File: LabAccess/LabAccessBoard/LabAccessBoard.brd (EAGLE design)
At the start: 43.2 x 62.2 mm, 26 parts, among them CN1 6p-2.54, Q1 AO3400, X1 1751248

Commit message: board update
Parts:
- removed C4: 100nF, rcl:C0603K
- removed CN1: 6p-2.54, Seeed-Connector:H6-2.54
- removed R1, R2, R7: 10k, resistor:R0603
- added J1: 4p-2.54, Seeed-Connector:H4-2.54
- moved R3 14.3 mm to (26.4, 32.7), turned to 0 degrees
- moved R6 8.80 mm to (26.4, 35.2), turned to 0 degrees
- moved C3 5.12 mm to (21.9, 38.4), turned to 90 degrees
- moved Q1 3.82 mm to (22.2, 26.7), turned to 90 degrees
- moved C1 2.86 mm to (22.2, 32.7), turned to 0 degrees
- moved D1 1.59 mm to (18.4, 30.8)
- moved R5 0.63 mm to (22.2, 30.2), turned to 180 degrees
- moved C6 0.32 mm to (26.4, 30.2)
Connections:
- removed net EN: C4.2, R7.2, U1.CH_PD
- removed net GPIO0: C4.1, CN1.6, R2.2, U1.GPIO0
- removed net RST: JP1.7, U1.RESET
- new net EXTSW: R6.2, U1.GPIO5, X1.2
- net +3V3: now also J1.4; no longer CN1.3, R2.1, R7.1
- net CS: now also U1.GPIO16; no longer R1.2, U1.GPIO15
- net GND: now also J1.1; no longer CN1.1, R1.1
- net RLY: now also U1.GPIO15; no longer U1.GPIO16
- net RX: now also J1.2; no longer CN1.4
- net SW: now also U1.GPIO0; no longer R6.2, U1.GPIO5, X1.2
- net TX: now also J1.3; no longer CN1.5
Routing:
- net EXTSW: track 0.00 -> 41.7 mm, vias 0 -> 1
- net SW: track 101.3 -> 67.7 mm
- net GPIO0: track 29.2 -> 0.00 mm
- net EN: track 23.5 -> 0.00 mm
- net RX: track 29.2 -> 22.6 mm
- net RLY: track 27.8 -> 32.6 mm
- net CS: track 63.5 -> 59.4 mm, vias 1 -> 2
- net N$8: track 13.5 -> 16.8 mm
- net TX: track 31.2 -> 28.1 mm
- net GPIO2: track 16.0 -> 18.4 mm
- net +3V3: track 71.6 -> 69.7 mm
- net N$5: track 28.4 -> 29.2 mm
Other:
- board text added: "3V3"
- board text added: "BOOT"
- board text added: "GND"
- board text added: "RX"
- board text added: "TX"

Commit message: board update
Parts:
- added IC1: TLP281, TLP281(GB-TP_F):SOIC127P700X190-4N
- added R1: (no value), resistor:R0603
- added R2, R7: 0, resistor:R0603
- C5: value (none) -> 100nF
- HLK-PM03: value HLK-PM013W -> HLK-PM03
- R4: value S07K250 -> 250V
- R5: value 2ohm -> 2R
- U$1: value SRD-0XVDC-SL-CSRD-06VDC-SL-C -> SRD-03VDC-SL-C
- U$2: value (none) -> 10mH
- moved C3 3.19 mm to (22.2, 35.2), turned to 0 degrees
- renumbered HLK1 to HLK-PM03
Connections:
- new net A: IC1.1, R2.1, X1.2
- new net K: IC1.2, R1.2, R7.1
- new net K': R1.1, X1.1
- net EXTSW: now also IC1.4, R2.2; no longer X1.2
- net GND: now also IC1.3, R7.2; no longer X1.1
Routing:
- net A: track 0.00 -> 33.6 mm, vias 0 -> 1
- net K: track 0.00 -> 26.1 mm, vias 0 -> 2
- net K': track 0.00 -> 6.71 mm
- net SW: track 67.7 -> 71.6 mm
- net GPIO2: track 18.4 -> 22.1 mm
- net EXTSW: track 41.7 -> 43.2 mm, vias 1 -> 2
- net IRQ: track 59.3 -> 58.0 mm
- net N$2: track 80.7 -> 81.2 mm
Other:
- outline, holes or cut-outs redrawn
- board text added: "+"
- board text added: "-"
- board text added: "F 0.5A"
- board text removed: "F125mA"

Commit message: board update
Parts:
- removed C3: 100nF, rcl:C0603K
- C1, C6: value 22uF -> 1uF; device rcl:C0805K -> rcl:C0603K
- C2: value 22uF -> 10uF
- D1: value 1N4007 -> 1N4001
- R1: value (none) -> ROC
- R6: value 3.3k -> RSW
- moved C6 5.40 mm to (26.4, 35.6)
- moved R5 5.40 mm to (22.2, 35.6)
- moved C2 4.45 mm to (40.3, 1.91)
- moved R3 3.18 mm to (26.4, 29.5)
- moved Q1 2.86 mm to (22.2, 29.5)
- moved R6 2.54 mm to (26.4, 32.7)
- moved IC1 0.48 mm to (34.0, 32.2)
- moved R2 0.48 mm to (34.9, 32.2)
- moved R7 0.48 mm to (33.0, 32.2)
- moved D1 0.45 mm to (18.1, 31.1)
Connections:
- removed net K': R1.1, X1.1
- new net N$9: R1.1, X1.2
- net +3V3: no longer C3.2
- net A: now also R1.2; no longer X1.2
- net GND: no longer C3.1
- net K: now also X1.1; no longer R1.2
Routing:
- net K: track 26.1 -> 38.0 mm, vias 2 -> 1
- net K': track 6.71 -> 0.00 mm
- net N$9: track 0.00 -> 6.18 mm
- net A: track 33.6 -> 29.9 mm, vias 1 -> 2
- net +3V3: track 69.6 -> 66.1 mm
- net GPIO2: track 22.1 -> 25.3 mm
- net EXTSW: track 43.2 -> 46.2 mm
- net N$8: track 16.8 -> 15.0 mm
- net RLY: track 32.6 -> 34.2 mm
- net N$5: track 28.9 -> 30.3 mm

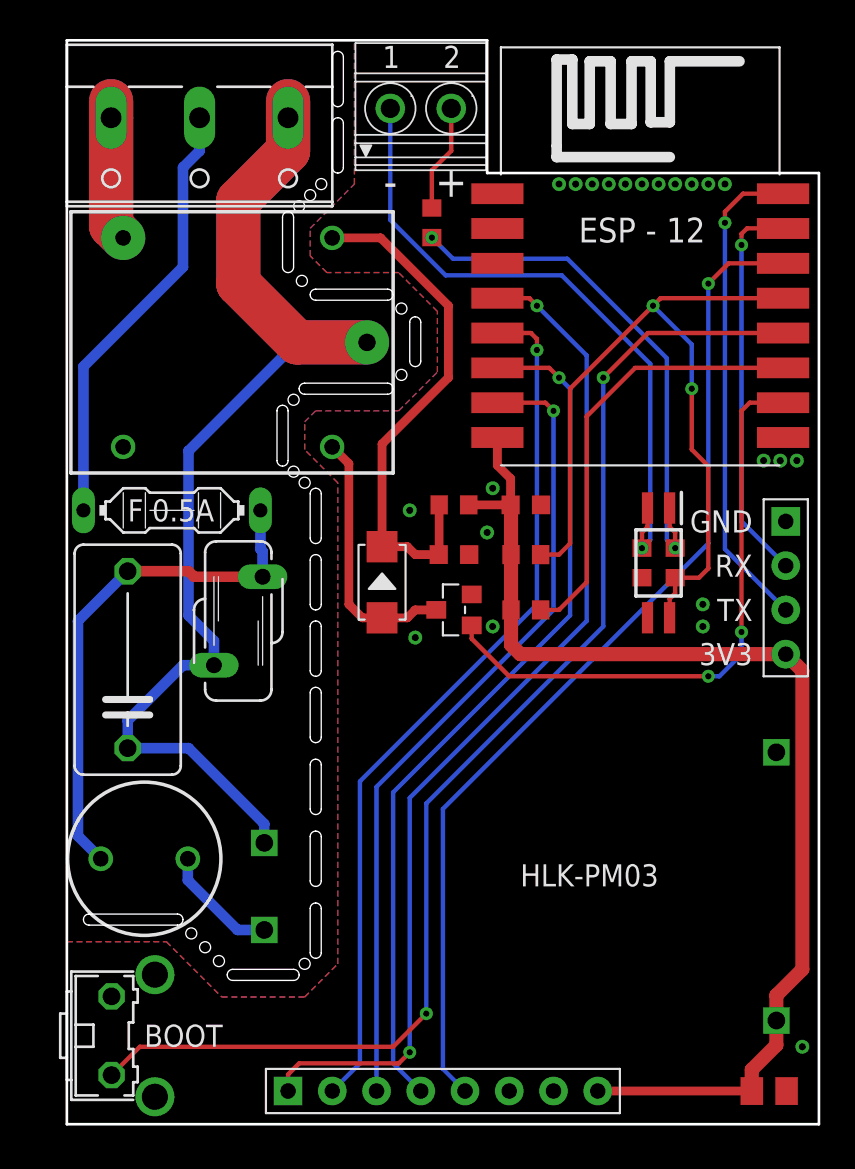
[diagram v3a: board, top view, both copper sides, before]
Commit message: new lab access board
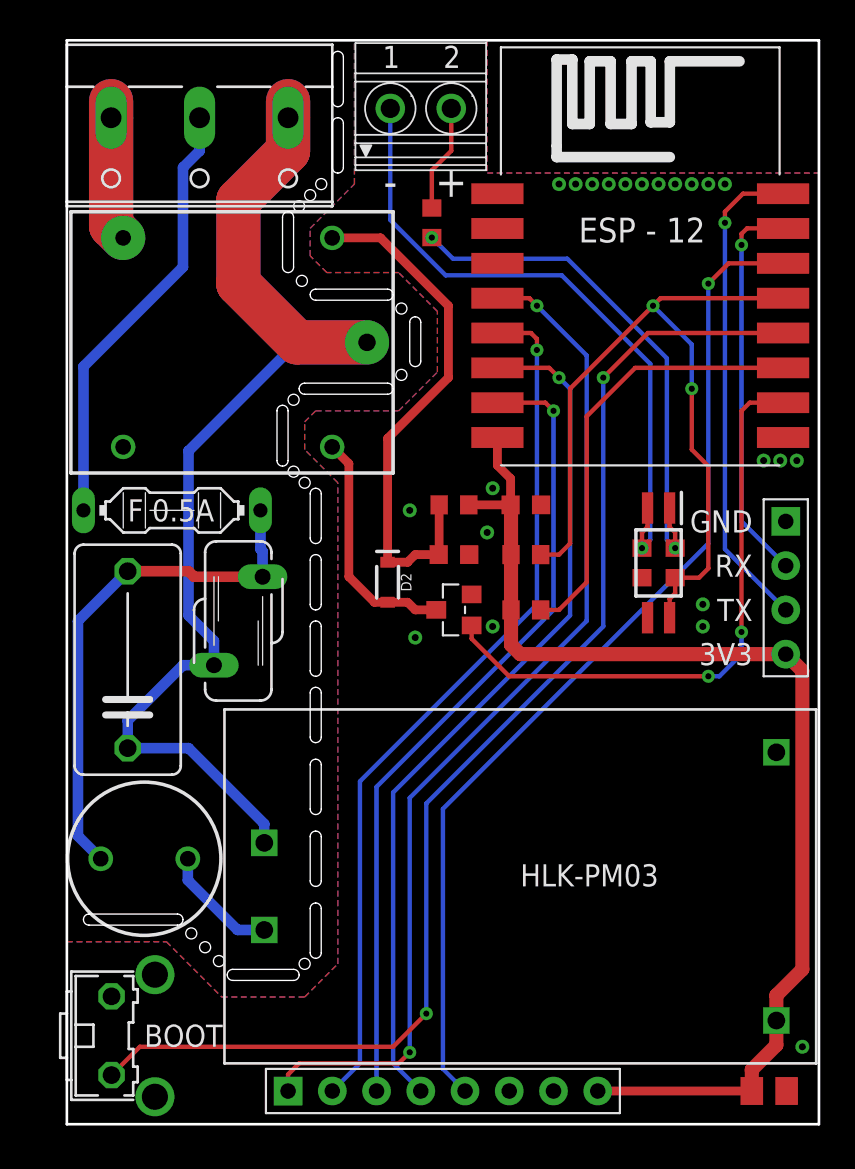
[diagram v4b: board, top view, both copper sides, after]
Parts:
- removed D1: 1N4001, Seeed-Diode:DO-214AC
- added D2: 250mA/100V, SparkFun-DiscreteSemi:SOD-323
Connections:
- net N$5: now also D2.C; no longer D1.2
- net N$8: now also D2.A; no longer D1.1
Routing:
- net N$8: track 15.0 -> 13.7 mm
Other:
- outline, holes or cut-outs redrawn
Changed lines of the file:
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@@
 <?xml version="1.0" encoding="utf-8"?>
 <!DOCTYPE eagle SYSTEM "eagle.dtd">
-<eagle version="9.0.1">
+<eagle version="9.2.2">
 <drawing>
 <settings>
@@
 <setting verticaltext="up"/>
 </settings>
-<grid distance="6.25" unitdist="mil" unit="mil" style="lines" multiple="1" display="yes" altdistance="5" altunitdist="mil" altunit="mil"/>
+<grid distance="12.5" unitdist="mil" unit="mil" style="lines" multiple="1" display="yes" altdistance="5" altunitdist="mil" altunit="mil"/>
 <layers>
 <layer number="1" name="Top" color="4" fill="1" visible="yes" active="yes"/>
@@
 <layer number="23" name="tOrigins" color="15" fill="1" visible="yes" active="yes"/>
 <layer number="24" name="bOrigins" color="15" fill="1" visible="yes" active="yes"/>
-<layer number="25" name="tNames" color="7" fill="1" visible="yes" active="yes"/>
+<layer number="25" name="tNames" color="7" fill="1" visible="no" active="yes"/>
 <layer number="26" name="bNames" color="7" fill="1" visible="yes" active="yes"/>
 <layer number="27" name="tValues" color="7" fill="1" visible="yes" active="yes"/>
@@
 <plain>
 <wire x1="0" y1="0" x2="0" y2="62.23" width="0.1524" layer="20"/>
-<wire x1="0" y1="62.23" x2="24.13" y2="62.23" width="0.1524" layer="20"/>
-<wire x1="24.13" y1="62.23" x2="24.13" y2="54.61" width="0.1524" layer="20"/>
-<wire x1="24.13" y1="54.61" x2="43.18" y2="54.61" width="0.1524" layer="20"/>
-<wire x1="43.18" y1="54.61" x2="43.18" y2="0" width="0.1524" layer="20"/>
+<wire x1="0" y1="62.23" x2="43.18" y2="62.23" width="0.1524" layer="20"/>
+<wire x1="43.18" y1="62.23" x2="43.18" y2="0" width="0.1524" layer="20"/>
 <wire x1="43.18" y1="0" x2="0" y2="0" width="0.1524" layer="20"/>
 <wire x1="6.35" y1="60.325" x2="9.525" y2="61.595" width="0.4064" layer="22"/>
@@
 <circle x="34.925" y="33.07715" radius="0.70995" width="0.508" layer="42"/>
 <wire x1="32.7025" y1="36.5125" x2="35.2425" y2="36.5125" width="0.508" layer="41"/>
+<wire x1="9.04875" y1="3.4925" x2="43.02125" y2="3.4925" width="0.1524" layer="21"/>
+<wire x1="43.02125" y1="3.4925" x2="43.02125" y2="23.8125" width="0.1524" layer="21"/>
+<wire x1="43.02125" y1="23.8125" x2="9.04875" y2="23.8125" width="0.1524" layer="21"/>
+<wire x1="9.04875" y1="23.8125" x2="9.04875" y2="3.4925" width="0.1524" layer="21"/>
+<rectangle x1="24.4475" y1="54.9275" x2="43.18" y2="62.23" layer="42"/>
+<rectangle x1="24.4475" y1="54.9275" x2="43.18" y2="62.23" layer="41"/>
 </plain>
 <attributes>
@@
 <param name="checkStop" value="0"/>
 <param name="checkValues" value="0"/>
+<param name="checkNames" value="1"/>
+<param name="checkWireStubs" value="1"/>
+<param name="checkPolygonWidth" value="0"/>
 <param name="useDiameter" value="13"/>
 <param name="maxErrors" value="50"/>
@@
 <attribute name="VALUE" x="20.16125" y="31.1785" size="0.8128" layer="27" font="vector" ratio="10"/>
 </element>
-<element name="D1" library="Seeed-Diode" library_urn="urn:adsk.eagle:library:467" package="DO-214AC" package3d_urn="urn:adsk.eagle:package:32508/1" value="1N4001" x="18.0975" y="31.115" smashed="yes" rot="R90">
-<attribute name="MPN" value="1N4007" x="18.0975" y="31.115" size="1.27" layer="27" font="vector" rot="R90" display="off"/>
-<attribute name="VALUE" x="16.51" y="28.8925" size="0.889" layer="27" font="vector" ratio="11" rot="R90"/>
-</element>
 <element name="R6" library="resistor" library_urn="urn:adsk.eagle:library:348" package="R0603" package3d_urn="urn:adsk.eagle:package:26057/1" value="RSW" x="26.3525" y="32.7025" smashed="yes">
 <attribute name="VALUE" x="25.0825" y="33.49625" size="1.016" layer="27" font="vector"/>
@@
 <attribute name="VALUE" x="25.3525" y="36.35875" size="1.016" layer="27" font="vector"/>
 </element>
-<element name="U$3" library="SparkFun-Aesthetics" library_urn="urn:adsk.eagle:library:507" package="OSHW-LOGO-L" package3d_urn="urn:adsk.eagle:package:37097/1" value="" x="29.21" y="18.7325" rot="MR0"/>
+<element name="U$3" library="SparkFun-Aesthetics" library_urn="urn:adsk.eagle:library:507" package="OSHW-LOGO-L" package3d_urn="urn:adsk.eagle:package:37097/1" value="" x="29.21" y="18.7325" smashed="yes" rot="MR0"/>
 <element name="J1" library="Seeed-Connector" library_urn="urn:adsk.eagle:library:478" package="H4-2.54" package3d_urn="urn:adsk.eagle:package:33137/1" value="4p-2.54" x="41.275" y="30.7975" smashed="yes">
 <attribute name="MPN" value="P125-1104A0BS116A1" x="41.275" y="30.7975" size="1.778" layer="27" display="off"/>
@@
 <element name="R2" library="resistor" library_urn="urn:adsk.eagle:library:348" package="R0603" package3d_urn="urn:adsk.eagle:package:26057/1" value="0" x="34.925" y="32.22625" smashed="yes" rot="R270"/>
 <element name="R7" library="resistor" library_urn="urn:adsk.eagle:library:348" package="R0603" package3d_urn="urn:adsk.eagle:package:26057/1" value="0" x="33.02" y="32.22625" smashed="yes" rot="R270"/>
+<element name="D2" library="SparkFun-DiscreteSemi" library_urn="urn:adsk.eagle:library:514" package="SOD-323" package3d_urn="urn:adsk.eagle:package:38441/1" value="250mA/100V" x="18.415" y="31.115" smashed="yes" rot="R270">
+<attribute name="NAME" x="19.177" y="31.115" size="0.6096" layer="25" font="vector" ratio="20" rot="R270" align="bottom-center"/>
+<attribute name="PROD_ID" value="DIO-09646" x="18.415" y="31.115" size="1.778" layer="27" rot="R270" display="off"/>
+</element>
 </elements>
 <signals>
@@
 <wire x1="38.735" y1="40.9575" x2="39.2025" y2="41.425" width="0.254" layer="1"/>
 <wire x1="36.83" y1="25.7175" x2="25.4" y2="25.7175" width="0.254" layer="1"/>
-<wire x1="23.241" y1="27.8765" x2="23.241" y2="28.6385" width="0.254" layer="1"/>
 <wire x1="25.4" y1="25.7175" x2="23.241" y2="27.8765" width="0.254" layer="1"/>
+<wire x1="23.241" y1="27.8765" x2="23.241" y2="28.6385" width="0.254" layer="1"/>
 </signal>
 <signal name="TX">
@@
 <contactref element="C1" pad="1"/>
 <contactref element="U$1" pad="COIL0"/>
-<contactref element="D1" pad="2"/>
 <wire x1="15.2325" y1="50.8875" x2="18.01" y2="50.8875" width="0.508" layer="1"/>
 <wire x1="18.01" y1="50.8875" x2="21.9075" y2="46.99" width="0.508" layer="1"/>
 <wire x1="21.9075" y1="46.99" x2="21.9075" y2="42.8625" width="0.508" layer="1"/>
-<wire x1="21.9075" y1="42.8625" x2="18.0975" y2="39.0525" width="0.508" layer="1"/>
-<wire x1="18.0975" y1="39.0525" x2="18.0975" y2="33.157" width="0.508" layer="1"/>
-<wire x1="21.375" y1="35.56" x2="21.375" y2="32.5525" width="0.508" layer="1"/>
+<wire x1="21.375" y1="35.56" x2="21.375" y2="32.7025" width="0.508" layer="1"/>
+<wire x1="21.375" y1="32.7025" x2="21.375" y2="32.5525" width="0.508" layer="1"/>
 <wire x1="21.375" y1="32.5525" x2="21.35" y2="32.7025" width="0.508" layer="1"/>
-<wire x1="19.548" y1="33.157" x2="18.0975" y2="33.157" width="0.508" layer="1"/>
-<wire x1="21.35" y1="32.7025" x2="20.0025" y2="32.7025" width="0.508" layer="1"/>
-<wire x1="20.0025" y1="32.7025" x2="19.548" y2="33.157" width="0.508" layer="1"/>
+<contactref element="D2" pad="C"/>
+<wire x1="18.415" y1="32.265" x2="19.565" y2="32.265" width="0.508" layer="1"/>
+<wire x1="19.565" y1="32.265" x2="20.0025" y2="32.7025" width="0.508" layer="1"/>
+<wire x1="20.0025" y1="32.7025" x2="21.375" y2="32.7025" width="0.508" layer="1"/>
+<wire x1="21.9075" y1="42.8625" x2="18.415" y2="39.37" width="0.508" layer="1"/>
+<wire x1="18.415" y1="39.37" x2="18.415" y2="32.265" width="0.508" layer="1"/>
 </signal>
 <signal name="N$8">
 <contactref element="U$1" pad="COIL1"/>
 <contactref element="Q1" pad="3"/>
-<contactref element="D1" pad="1"/>
 <wire x1="15.2325" y1="38.8875" x2="16.1925" y2="37.9275" width="0.508" layer="1"/>
-<wire x1="16.1925" y1="37.9275" x2="16.1925" y2="29.845" width="0.508" layer="1"/>
-<wire x1="16.1925" y1="29.845" x2="16.9645" y2="29.073" width="0.508" layer="1"/>
-<wire x1="16.9645" y1="29.073" x2="18.0975" y2="29.073" width="0.508" layer="1"/>
-<wire x1="21.209" y1="29.5275" x2="20.0025" y2="29.5275" width="0.508" layer="1"/>
-<wire x1="19.548" y1="29.073" x2="18.0975" y2="29.073" width="0.508" layer="1"/>
-<wire x1="20.0025" y1="29.5275" x2="19.548" y2="29.073" width="0.508" layer="1"/>
+<contactref element="D2" pad="A"/>
+<wire x1="16.1925" y1="37.9275" x2="16.1925" y2="31.4325" width="0.508" layer="1"/>
+<wire x1="17.66" y1="29.965" x2="18.415" y2="29.965" width="0.508" layer="1"/>
+<wire x1="16.1925" y1="31.4325" x2="17.66" y2="29.965" width="0.508" layer="1"/>
+<wire x1="18.415" y1="29.965" x2="19.565" y2="29.965" width="0.508" layer="1"/>
+<wire x1="19.565" y1="29.965" x2="20.0025" y2="29.5275" width="0.508" layer="1"/>
+<wire x1="20.0025" y1="29.5275" x2="21.209" y2="29.5275" width="0.508" layer="1"/>
 </signal>
 <signal name="N$6">
@@
 </signal>
 </signals>
+<mfgpreviewcolors>
+<mfgpreviewcolor name="soldermaskcolor" color="0xC8008000"/>
+<mfgpreviewcolor name="silkscreencolor" color="0xFFFEFEFE"/>
+<mfgpreviewcolor name="backgroundcolor" color="0xFF282828"/>
+<mfgpreviewcolor name="coppercolor" color="0xFFFFBF00"/>
+<mfgpreviewcolor name="substratecolor" color="0xFF786E46"/>
+</mfgpreviewcolors>
 </board>
 </drawing>
